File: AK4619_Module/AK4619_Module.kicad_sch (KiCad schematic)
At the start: 58 parts, among them J1 Conn_01x02, J2 AudioJack2_Ground, J3 AudioJack2_Ground, J4 Conn_01x11, J5 AudioJack2_Ground, J6 AudioJack2_Ground, SW1 SKRPABE010, U1 AP7361EA-33E-13, U2 AK4619VN, U3 ADM811TARTZ

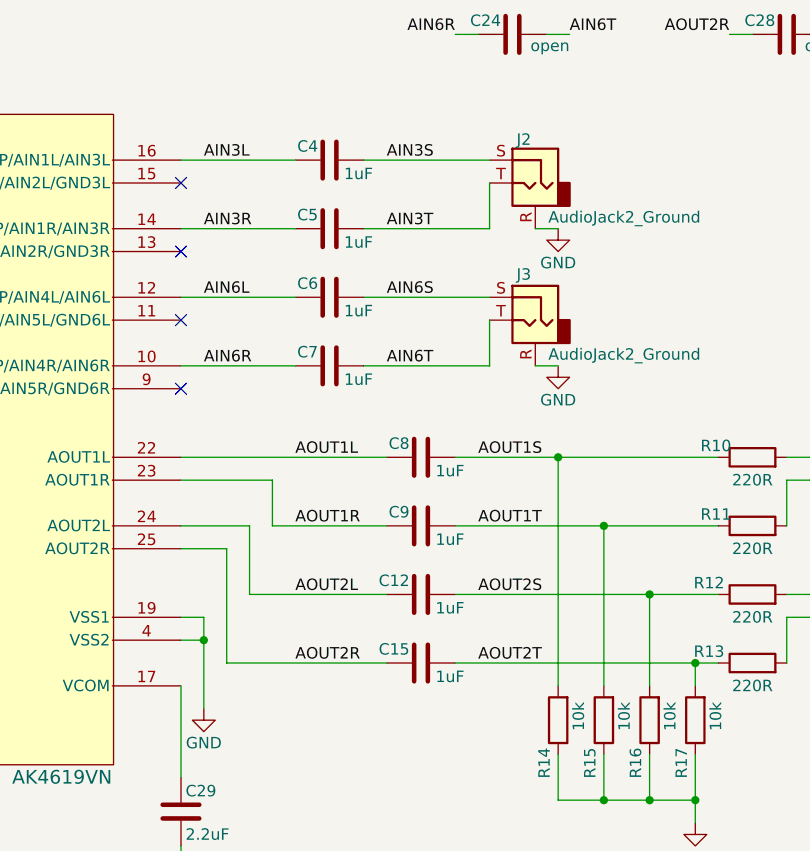
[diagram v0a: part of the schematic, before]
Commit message: C4,5,6,7,8,9,12,15の値を修正
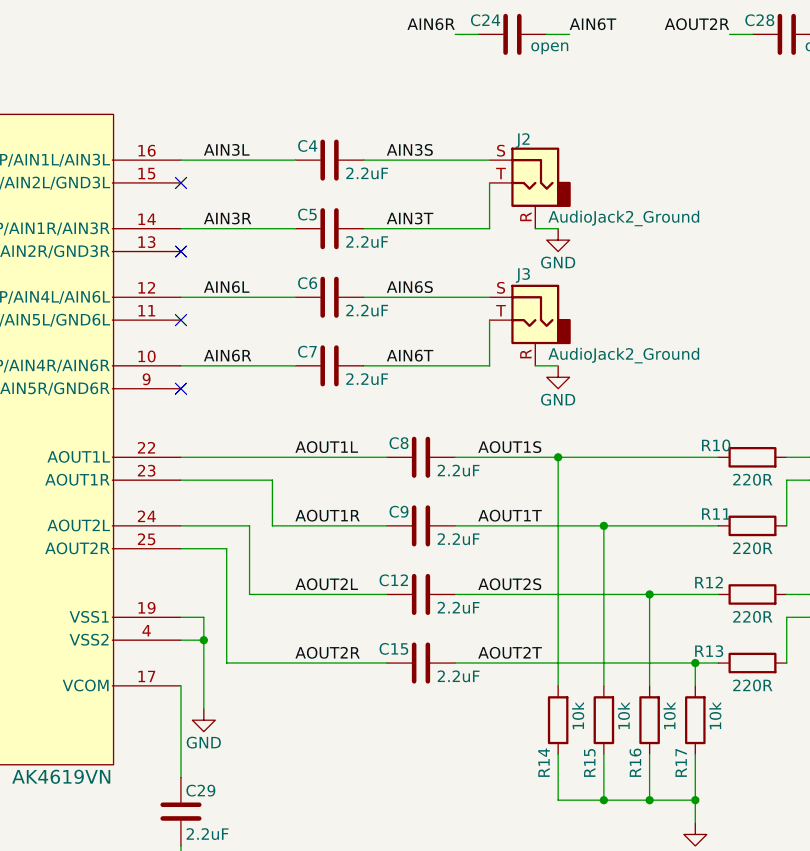
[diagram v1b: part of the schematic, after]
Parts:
- C12, C15, C4, C5, C6, C7, C8, C9: value 1uF -> 2.2uF
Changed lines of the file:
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@@
 			)
 		)
-		(property "Value" "1uF"
-			(at 214.376 101.854 90)
+		(property "Value" "2.2uF"
+			(at 216.154 101.854 90)
 			(effects
 				(font
@@
 			)
 		)
-		(property "Value" "1uF"
-			(at 214.376 94.234 90)
+		(property "Value" "2.2uF"
+			(at 216.154 94.234 90)
 			(effects
 				(font
@@
 			)
 		)
-		(property "Value" "1uF"
-			(at 224.536 134.874 90)
+		(property "Value" "2.2uF"
+			(at 226.314 134.874 90)
 			(effects
 				(font
@@
 			)
 		)
-		(property "Value" "1uF"
-			(at 224.536 112.014 90)
+		(property "Value" "2.2uF"
+			(at 226.314 112.014 90)
 			(effects
 				(font
@@
 			)
 		)
-		(property "Value" "1uF"
-			(at 214.376 86.614 90)
+		(property "Value" "2.2uF"
+			(at 216.154 86.614 90)
 			(effects
 				(font
@@
 			)
 		)
-		(property "Value" "1uF"
-			(at 214.376 78.994 90)
+		(property "Value" "2.2uF"
+			(at 216.154 78.994 90)
 			(effects
 				(font
@@
 			)
 		)
-		(property "Value" "1uF"
-			(at 224.536 127.254 90)
+		(property "Value" "2.2uF"
+			(at 226.314 127.254 90)
 			(effects
 				(font
@@
 			)
 		)
-		(property "Value" "1uF"
-			(at 224.536 119.634 90)
-			(effects
-				(font
+		(property "Value" "2.2uF"
+			(at 226.314 119.634 90)
+			(effects
+				(font
